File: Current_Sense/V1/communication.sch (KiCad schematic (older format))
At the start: 28 parts, among them J301 1694224, J302 1694240, U301 SI8422AB-D-IS, U302 SN65HVD232DR

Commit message: start to place pin on uC
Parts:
- removed J301: 1694224, Connectors:1694224, symbol 1694224
- removed J302: 1694240, Connectors:1694240, symbol 1694240
- added J301, J302: 649006227222, Connectors:649006227222, symbol 649006227222
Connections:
- net labels added: Shield1
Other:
- moved on the sheet: C302, C303, C310, C311, D301, D302, R301, R307

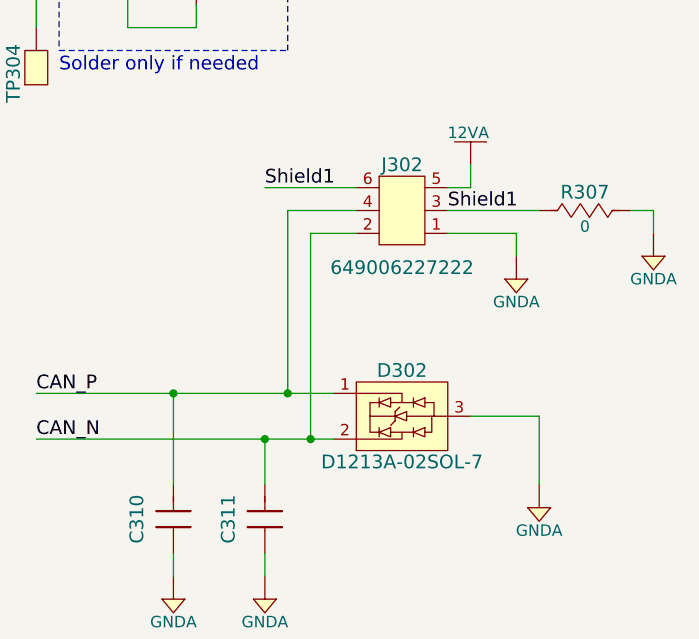
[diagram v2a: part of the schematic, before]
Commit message: routing uC
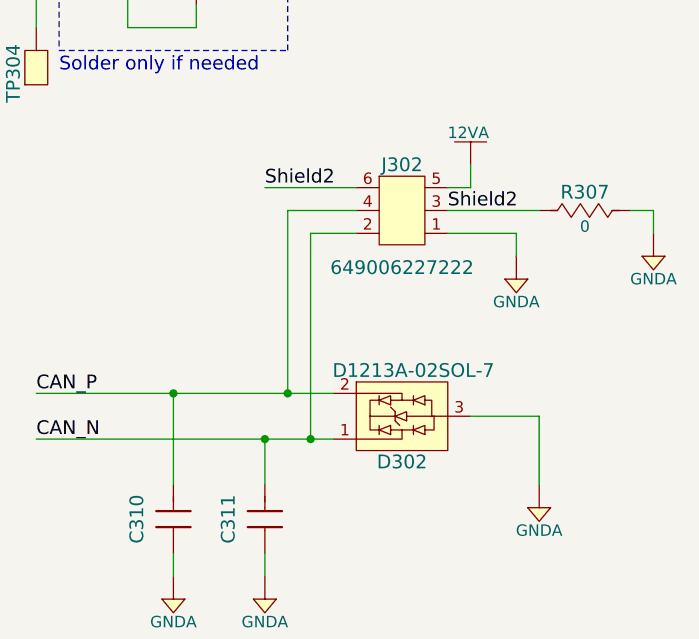
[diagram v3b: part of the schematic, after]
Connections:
- net CAN_N: now also D302.1 (CH1); no longer D302.2 (CH2)
- net CAN_P: now also D302.2 (CH2); no longer D302.1 (CH1)
- net Shield1: no longer J302.3, J302.6, R307.1
- new net Shield2: J302.3, J302.6, R307.1
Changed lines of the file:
@@
 P 9200 5600
 F 0 "D302" H 9200 5800 60  0000 C CNN
-F 1 "D1213A-02SOL-7" H 9200 5400 60  0000 C CNN
+F 1 "D1213A-02SOL-7" H 9250 5400 60  0000 C CNN
 F 2 "IC:SOT-23-3" H 9200 4580 60  0001 C CNN
 F 3 "https://www.diodes.com/assets/Datasheets/D1213A_02SOL.pdf" H 9200 4480 60  0001 C CNN
@@
 F 8 "TVS DIODE 3.3VWM 10VC SOT23" H 9200 4680 60  0001 C CNN "Description"
 	1    9200 5600
-	1    0    0    -1
+	1    0    0    1
 $EndComp
 $Comp
@@
 	9500 4600 9400 4600
 Text Label 9400 4700 0    60   ~ 0
-Shield1
+Shield2
 Text Label 8600 4600 0    60   ~ 0
-Shield1
+Shield2
 Wire Wire Line
 	8600 4600 9000 4600

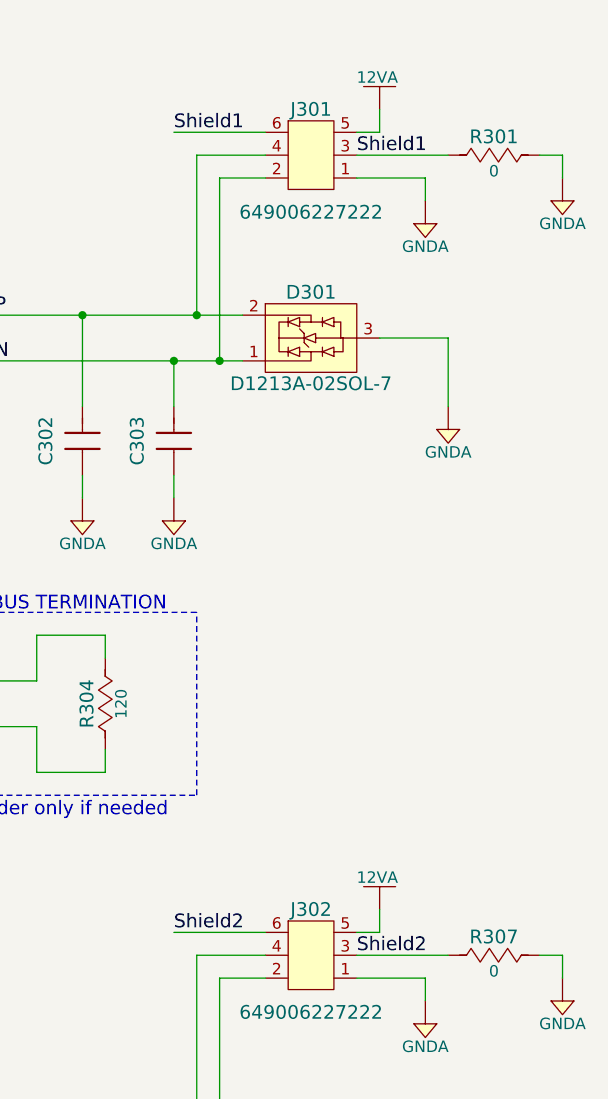
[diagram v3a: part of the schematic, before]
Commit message: board done, DRC clean
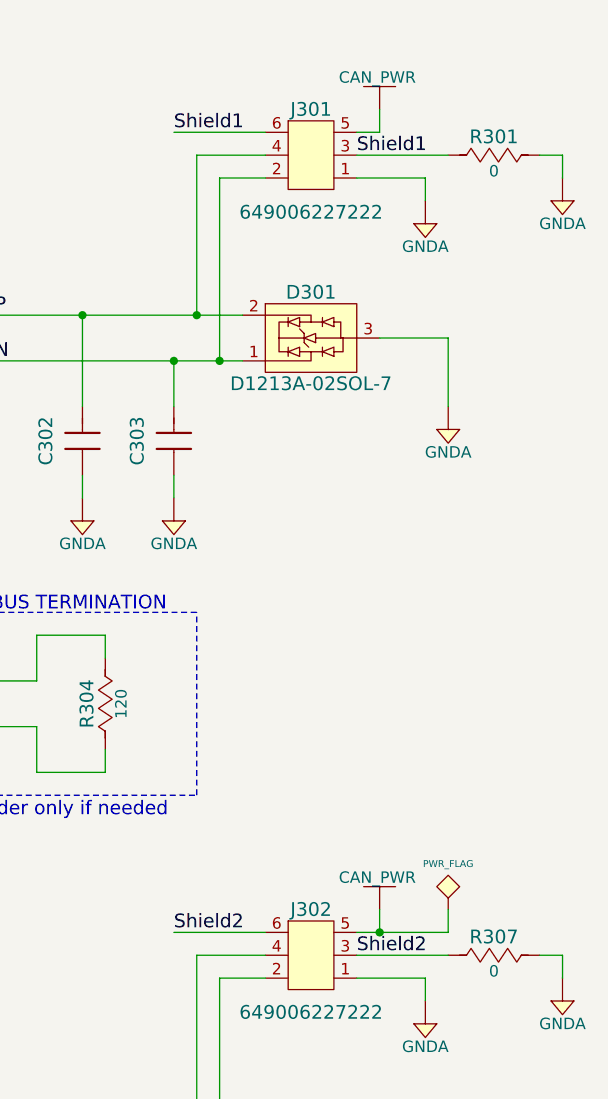
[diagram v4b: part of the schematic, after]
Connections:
- net 12VA renamed CAN_PWR
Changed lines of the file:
@@
-$EndComp
-$Comp
-L 12VA #PWR039
-U 1 1 592F3CEA
-P 9500 1000
-F 0 "#PWR039" H 9500 850 50  0001 C CNN
-F 1 "12VA" H 9490 1140 50  0000 C CNN
-F 2 "" H 9500 1000 60  0000 C CNN
-F 3 "" H 9500 1000 60  0000 C CNN
-	1    9500 1000
-	1    0    0    -1
 $EndComp
 $Comp
@@
 $EndComp
 $Comp
-L GNDA #PWR040
+L GNDA #PWR039
 U 1 1 592F3CFE
 P 8200 2800
-F 0 "#PWR040" H 8200 2630 50  0001 C CNN
+F 0 "#PWR039" H 8200 2630 50  0001 C CNN
 F 1 "GNDA" H 8200 2700 50  0000 C CNN
 F 2 "" H 8200 2900 60  0000 C CNN
@@
 $EndComp
 $Comp
-L GNDA #PWR041
+L GNDA #PWR040
 U 1 1 592F3D04
 P 8600 2800
-F 0 "#PWR041" H 8600 2630 50  0001 C CNN
+F 0 "#PWR040" H 8600 2630 50  0001 C CNN
 F 1 "GNDA" H 8600 2700 50  0000 C CNN
 F 2 "" H 8600 2900 60  0000 C CNN
@@
 	1900 3500 1900 2500
 $Comp
-L GNDB #PWR042
+L GNDB #PWR041
 U 1 1 592F3A57
 P 1600 4300
-F 0 "#PWR042" H 1600 4130 50  0001 C CNN
+F 0 "#PWR041" H 1600 4130 50  0001 C CNN
 F 1 "GNDB" H 1600 4200 50  0000 C CNN
 F 2 "" H 1600 4400 60  0000 C CNN
@@
 $EndComp
 $Comp
-L GNDB #PWR043
+L GNDB #PWR042
 U 1 1 592F3A7B
 P 2400 2800
-F 0 "#PWR043" H 2400 2630 50  0001 C CNN
+F 0 "#PWR042" H 2400 2630 50  0001 C CNN
 F 1 "GNDB" H 2400 2700 50  0000 C CNN
 F 2 "" H 2400 2900 60  0000 C CNN
@@
 	10300 1200 10200 1200
 $Comp
-L GNDA #PWR044
+L GNDA #PWR043
 U 1 1 595BE480
 P 9700 1500
-F 0 "#PWR044" H 9700 1330 50  0001 C CNN
+F 0 "#PWR043" H 9700 1330 50  0001 C CNN
 F 1 "GNDA" H 9700 1400 50  0000 C CNN
 F 2 "" H 9700 1600 60  0000 C CNN
@@
 	9000 1300 8800 1300
 $Comp
-L GNDA #PWR045
+L GNDA #PWR044
 U 1 1 595BF908
 P 10300 4900
-F 0 "#PWR045" H 10300 4730 50  0001 C CNN
+F 0 "#PWR044" H 10300 4730 50  0001 C CNN
 F 1 "GNDA" H 10300 4800 50  0000 C CNN
 F 2 "" H 10300 5000 60  0000 C CNN
 F 3 "" H 10280 4810 60  0000 C CNN
 	1    10300 4900
-	1    0    0    -1
-$EndComp
-$Comp
-L 12VA #PWR046
-U 1 1 595BF90E
-P 9500 4500
-F 0 "#PWR046" H 9500 4350 50  0001 C CNN
-F 1 "12VA" H 9490 4640 50  0000 C CNN
-F 2 "" H 9500 4500 60  0000 C CNN
-F 3 "" H 9500 4500 60  0000 C CNN
-	1    9500 4500
 	1    0    0    -1
 $EndComp
@@
 	10300 4700 10200 4700
 $Comp
-L GNDA #PWR047
+L GNDA #PWR045
 U 1 1 595BF931
 P 9700 5000
-F 0 "#PWR047" H 9700 4830 50  0001 C CNN
+F 0 "#PWR045" H 9700 4830 50  0001 C CNN
 F 1 "GNDA" H 9700 4900 50  0000 C CNN
 F 2 "" H 9700 5100 60  0000 C CNN
@@
 	9500 4500 9500 4600
 Wire Wire Line
-	9500 4600 9400 4600
+	9400 4600 9800 4600
 Text Label 9400 4700 0    60   ~ 0
 Shield2
@@
 Wire Wire Line
 	9000 4800 8800 4800
+$Comp
+L CAN_PWR #PWR046
+U 1 1 595D7366
+P 9500 1000
+F 0 "#PWR046" H 9500 850 50  0001 C CNN
+F 1 "CAN_PWR" H 9490 1140 50  0000 C CNN
+F 2 "" H 9500 1000 60  0000 C CNN
+F 3 "" H 9500 1000 60  0000 C CNN
+	1    9500 1000
+	1    0    0    -1
+$EndComp
+$Comp
+L CAN_PWR #PWR047
+U 1 1 595D7811
+P 9500 4500
+F 0 "#PWR047" H 9500 4350 50  0001 C CNN
+F 1 "CAN_PWR" H 9490 4640 50  0000 C CNN
+F 2 "" H 9500 4500 60  0000 C CNN
+F 3 "" H 9500 4500 60  0000 C CNN
+	1    9500 4500
+	1    0    0    -1
+$EndComp
+$Comp
+L PWR_FLAG #FLG048
+U 1 1 595D9EDA
+P 9800 4500
+F 0 "#FLG048" H 9800 4400 60  0001 C CNN
+F 1 "PWR_FLAG" H 9800 4700 30  0000 C CNN
+F 2 "" H 9800 4500 60  0000 C CNN
+F 3 "" H 9800 4500 60  0000 C CNN
+	1    9800 4500
+	1    0    0    -1
+$EndComp
+Wire Wire Line
+	9800 4600 9800 4500
+Connection ~ 9500 4600
 $EndSCHEMATC
